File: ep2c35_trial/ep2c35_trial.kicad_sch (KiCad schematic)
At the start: 144 parts, among them J1 Conn_02x21_Odd_Even, J2 Conn_02x21_Odd_Even, J3 3M_8540-4500PL, J4 USB3_B_Micro_Amphenol_GSB343K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, J5 Conn_02x05_Odd_Even, J6 Conn_01x02_Male, J7 Conn_01x02_Male, J8 Conn_01x02_Male, J9 Conn_01x02_Male, U1 EP2C5F484, U2 MIC37302, U3 FT600Q-B-T, U4 W25Q16JVSNIQ, U5 MIC39102, U6 MIC49150-1.2, X1 FNETHE025, Y1 ABM7-30.000MHZ-D2Y-T

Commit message: Add lvds_tx.
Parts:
- added D4, D5, D6, D7: LED, LED_SMD:LED_0603_1608Metric, symbol Device:LED
- added J10: Conn_02x10_Odd_Even, Connector_PinHeader_1.27mm:PinHeader_2x10_P1.27mm_Horizontal, symbol Connector_Generic:Conn_02x10_Odd_Even
- added R52, R53, R54, R55: 1k, Resistor_SMD:R_0402_1005Metric, symbol Device:R
- added R56, R58, R59, R61, R62, R64, R65, R67: 120, Resistor_SMD:R_0402_1005Metric, symbol Device:R
- added R57, R60, R63, R66: 170, Resistor_SMD:R_0402_1005Metric, symbol Device:R
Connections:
- net GND: now also J10.1 (Pin_1), J10.10 (Pin_10), J10.12 (Pin_12), J10.14 (Pin_14), J10.16 (Pin_16), J10.18 (Pin_18), J10.19 (Pin_19), J10.2 (Pin_2), J10.20 (Pin_20), J10.4 (Pin_4), J10.6 (Pin_6), J10.8 (Pin_8), R52.1, R53.1, R54.1, R55.1
- net LED0: now reaches U1.G1 (IO/LVDS31p)
- net LED0: now also D4.2 (A)
- net LED1: now reaches U1.G2 (IO/LVDS31n)
- net LED1: now also D5.2 (A)
- net LED2: now reaches U1.H1 (IO/LVDS29p)
- net LED2: now also D6.2 (A)
- net LED3: now reaches U1.H2 (IO/LVDS29n)
- net LED3: now also D7.2 (A)
- net LVDS_TX_DATA0_RAW_N: now reaches U1.AA10 (IO/LVDS178n)
- net LVDS_TX_DATA0_RAW_N: now also R56.2
- net LVDS_TX_DATA3_RAW_N: now reaches U1.AA7 (IO/LVDS189n)
- net LVDS_TX_DATA3_RAW_N: now also R65.2
- net LVDS_TX_DATA2_RAW_N: now reaches U1.AA8 (IO/LVDS183n)
- net LVDS_TX_DATA2_RAW_N: now also R62.2
- net LVDS_TX_DATA1_RAW_N: now reaches U1.AA9 (IO/LVDS181n)
- net LVDS_TX_DATA1_RAW_N: now also R59.2
- net LVDS_TX_DATA0_RAW_P: now reaches U1.AB10 (IO/LVDS178p)
- net LVDS_TX_DATA0_RAW_P: now also R58.2
- net LVDS_TX_DATA3_RAW_P: now reaches U1.AB7 (IO/LVDS189p)
- net LVDS_TX_DATA3_RAW_P: now also R67.2
- net LVDS_TX_DATA2_RAW_P: now reaches U1.AB8 (IO/LVDS183p)
- net LVDS_TX_DATA2_RAW_P: now also R64.2
- net LVDS_TX_DATA1_RAW_P: now reaches U1.AB9 (IO/LVDS181p)
- net LVDS_TX_DATA1_RAW_P: now also R61.2
- new net: D7.1 (K), R55.2
- new net: D6.1 (K), R54.2
- new net: D5.1 (K), R53.2
- new net: D4.1 (K), R52.2
- new net LVDS_TX_DATA0_N: J10.5 (Pin_5), R56.1, R57.2
- new net LVDS_TX_DATA0_P: J10.3 (Pin_3), R57.1, R58.1
- new net LVDS_TX_DATA1_N: J10.9 (Pin_9), R59.1, R60.2
- new net LVDS_TX_DATA1_P: J10.7 (Pin_7), R60.1, R61.1
- new net LVDS_TX_DATA2_N: J10.13 (Pin_13), R62.1, R63.2
- new net LVDS_TX_DATA2_P: J10.11 (Pin_11), R63.1, R64.1
- new net LVDS_TX_DATA3_N: J10.17 (Pin_17), R65.1, R66.2
- new net LVDS_TX_DATA3_P: J10.15 (Pin_15), R66.1, R67.1
- no-connect marks 196 -> 184

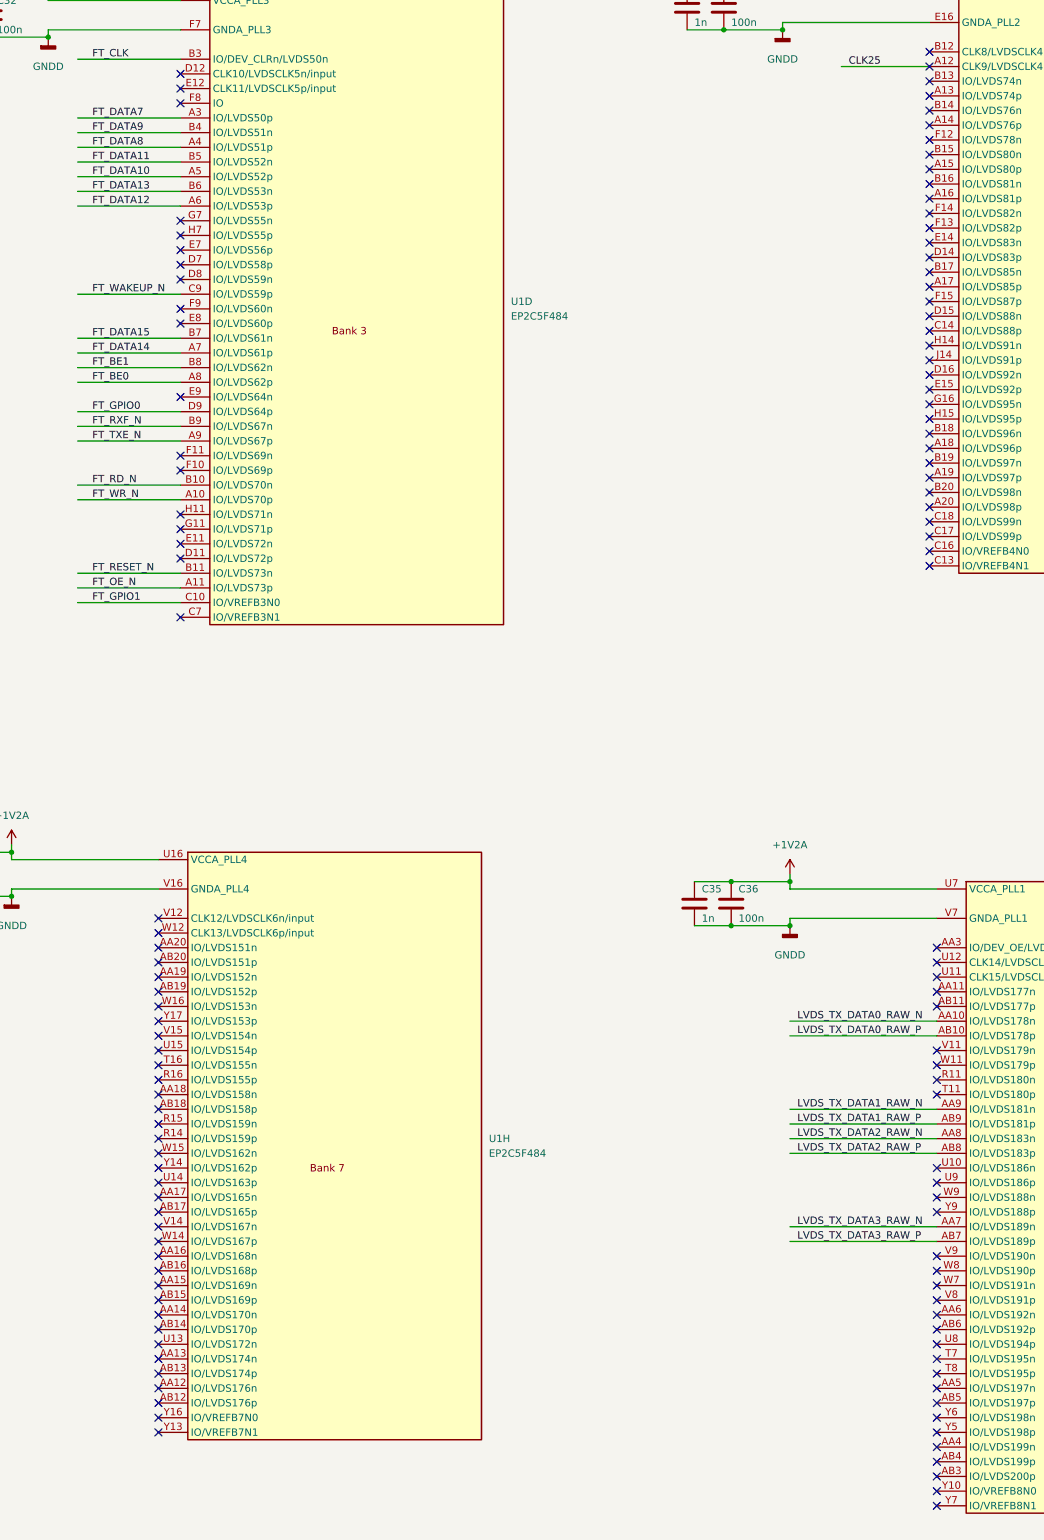
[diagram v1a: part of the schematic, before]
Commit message: Top ground plan.
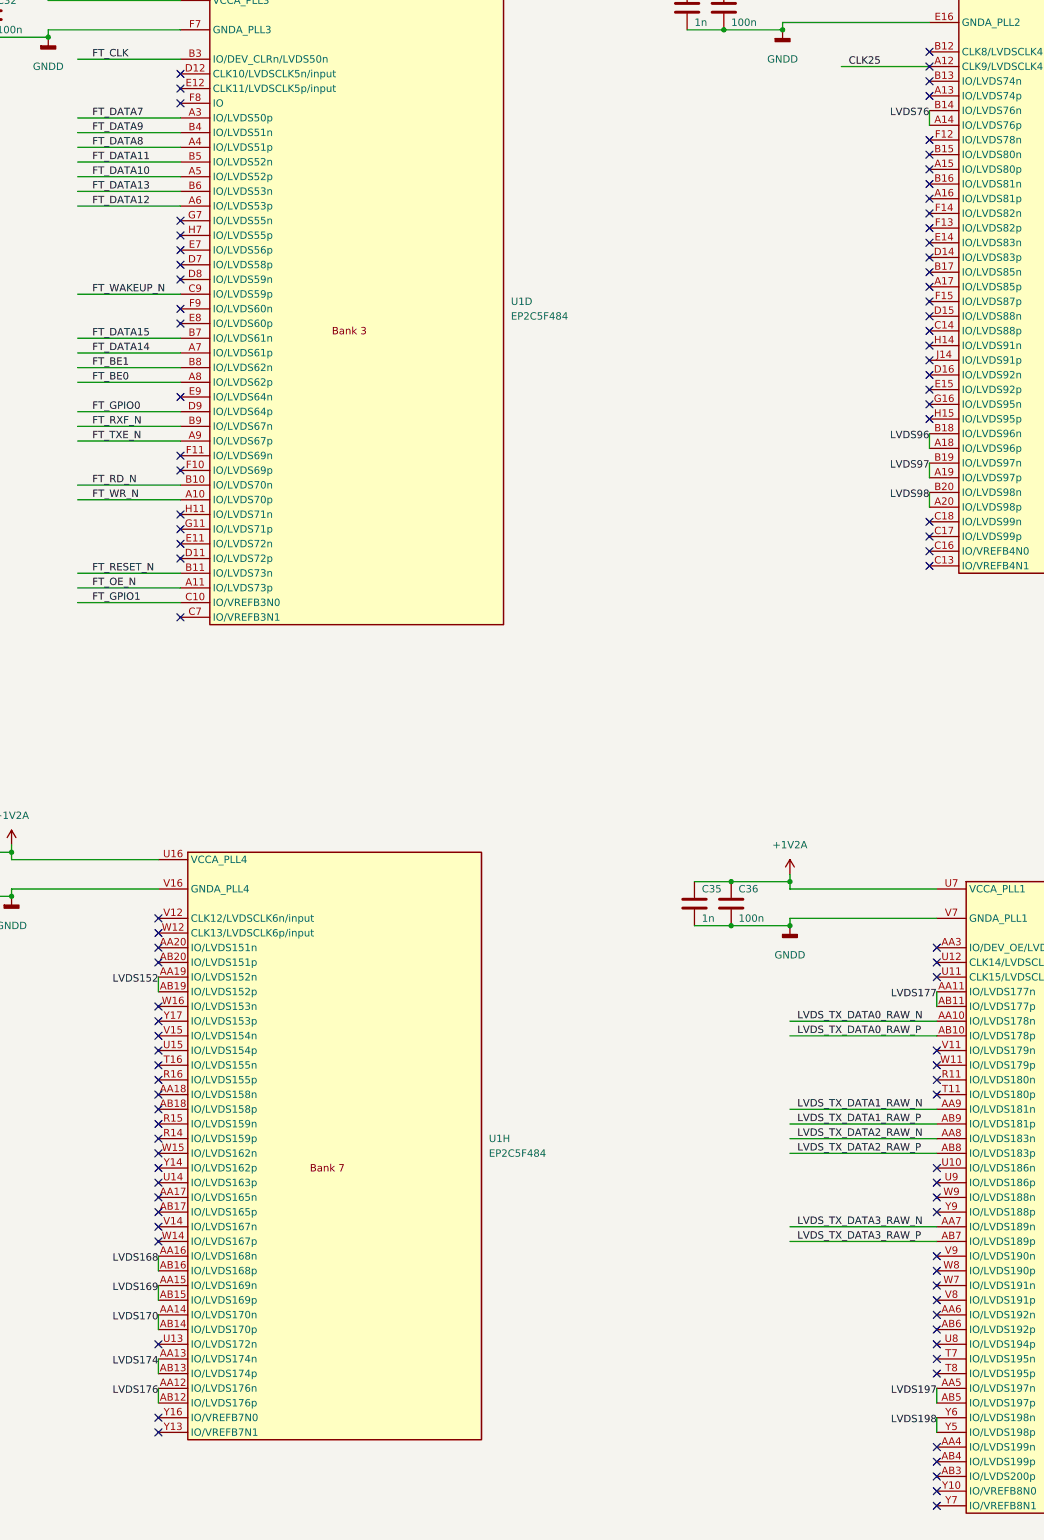
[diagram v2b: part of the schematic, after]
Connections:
- net LVDS76: now reaches U1.A14 (IO/LVDS76p)
- net LVDS76: now also U1.B14 (IO/LVDS76n)
- net LVDS96: now reaches U1.A18 (IO/LVDS96p)
- net LVDS96: now also U1.B18 (IO/LVDS96n)
- net LVDS97: now reaches U1.A19 (IO/LVDS97p)
- net LVDS97: now also U1.B19 (IO/LVDS97n)
- net LVDS98: now reaches U1.A20 (IO/LVDS98p)
- net LVDS98: now also U1.B20 (IO/LVDS98n)
- net LVDS176: now reaches U1.AA12 (IO/LVDS176n)
- net LVDS176: now also U1.AB12 (IO/LVDS176p)
- net LVDS174: now reaches U1.AA13 (IO/LVDS174n)
- net LVDS174: now also U1.AB13 (IO/LVDS174p)
- net LVDS170: now reaches U1.AA14 (IO/LVDS170n)
- net LVDS170: now also U1.AB14 (IO/LVDS170p)
- net LVDS169: now reaches U1.AA15 (IO/LVDS169n)
- net LVDS169: now also U1.AB15 (IO/LVDS169p)
- net LVDS168: now reaches U1.AA16 (IO/LVDS168n)
- net LVDS168: now also U1.AB16 (IO/LVDS168p)
- net LVDS152: now reaches U1.AA19 (IO/LVDS152n)
- net LVDS152: now also U1.AB19 (IO/LVDS152p)
- net LVDS177: now reaches U1.AA11 (IO/LVDS177n)
- net LVDS177: now also U1.AB11 (IO/LVDS177p)
- net LVDS197: now reaches U1.AA5 (IO/LVDS197n)
- net LVDS197: now also U1.AB5 (IO/LVDS197p)
- net LVDS198: now reaches U1.Y5 (IO/LVDS198p)
- net LVDS198: now also U1.Y6 (IO/LVDS198n)
- no-connect marks 184 -> 158

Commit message: Add ESD protection.
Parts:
- added U10, U11, U12, U13, U14, U15, U16, U7, U8, U9: SP3003-02UTG, Package_TO_SOT_SMD:SOT-23-6, symbol logic_analyzer:SP3003-02UTG
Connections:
- net GND: now also U10.3, U10.4, U11.3, U11.4, U12.3, U12.4, U13.3, U13.4, U14.3, U14.4, U15.3, U15.4, U16.1, U16.3, U16.4, U16.6, U7.3, U7.4, U8.3, U8.4, U9.3, U9.4
- net POD_CLK: now also U16.2, U16.5
- net POD_D0: now also U8.2, U8.5
- net POD_D1: now also U8.1, U8.6
- net POD_D10: now also U13.2, U13.5
- net POD_D11: now also U13.1, U13.6
- net POD_D12: now also U14.2, U14.5
- net POD_D13: now also U14.1, U14.6
- net POD_D14: now also U15.2, U15.5
- net POD_D15: now also U15.1, U15.6
- net POD_D2: now also U9.2, U9.5
- net POD_D3: now also U9.1, U9.6
- net POD_D4: now also U10.2, U10.5
- net POD_D5: now also U10.1, U10.6
- net POD_D6: now also U11.2, U11.5
- net POD_D7: now also U11.1, U11.6
- net POD_D8: now also U12.2, U12.5
- net POD_D9: now also U12.1, U12.6
- net USB_D_N: now also U7.1, U7.6
- net USB_D_P: now also U7.2, U7.5
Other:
- moved on the sheet: D4, D5, D6, D7, J3, R32, R33, R34, R35, R36, R37, R38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
